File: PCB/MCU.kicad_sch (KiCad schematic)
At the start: 15 parts

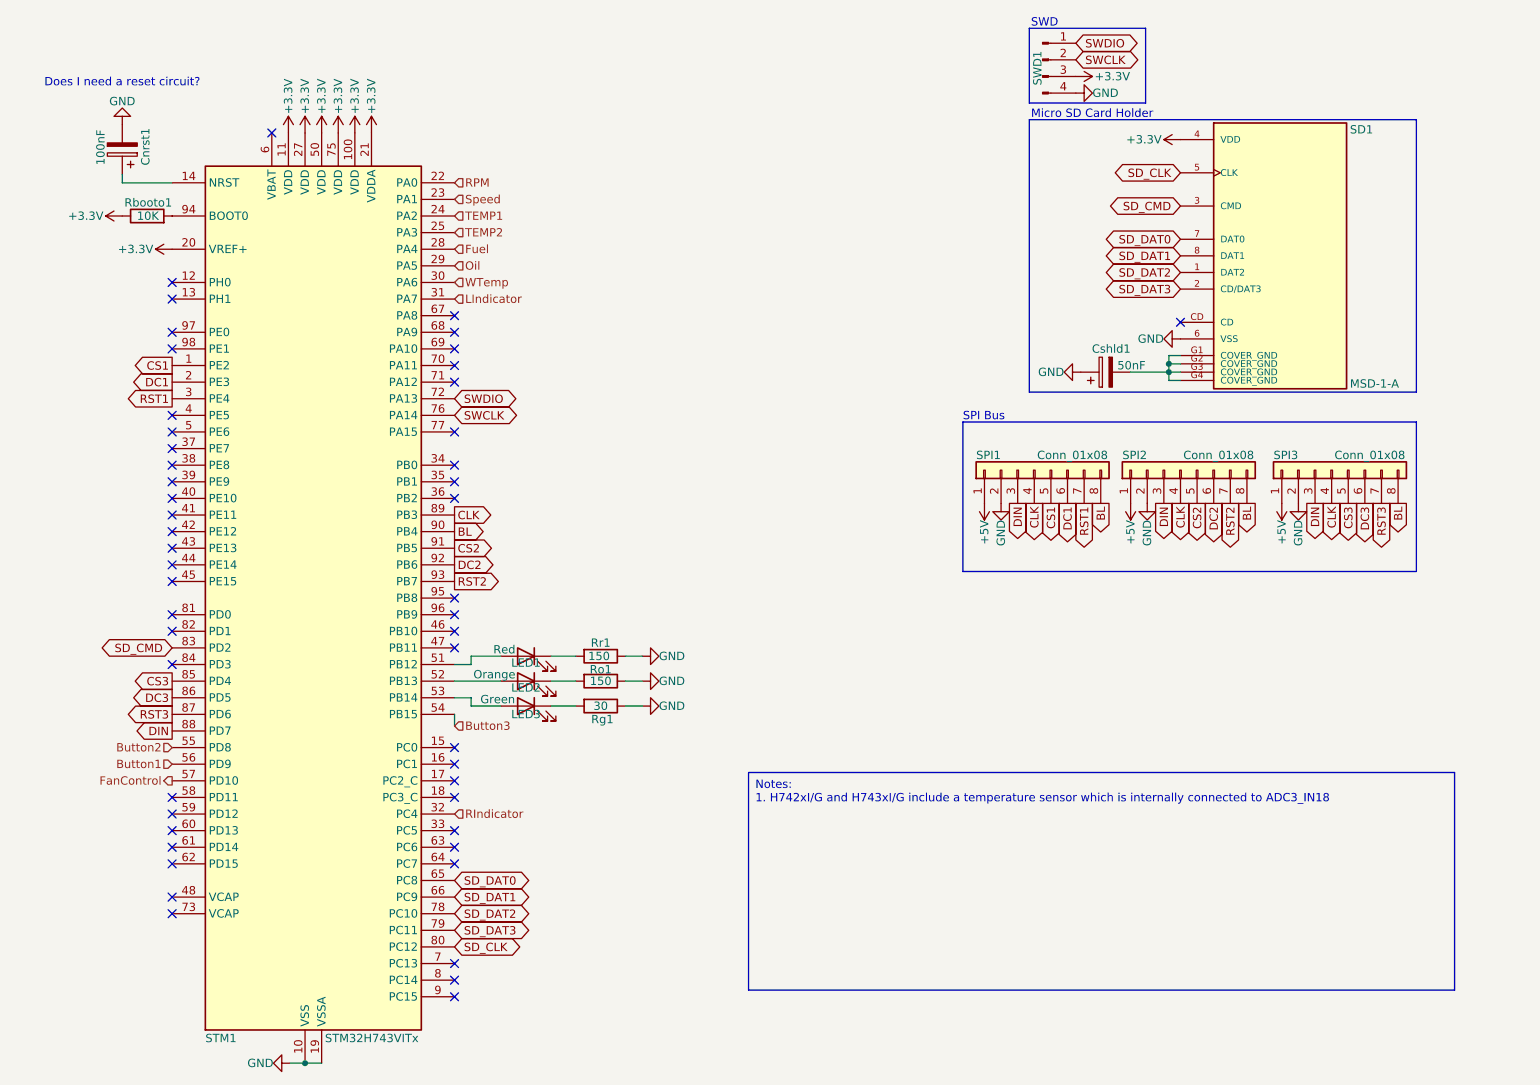
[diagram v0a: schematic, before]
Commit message: Replaced STM32 with ESP32; Addec circuitry for ESP32; Removed LEDs; Added USB-C for flashing
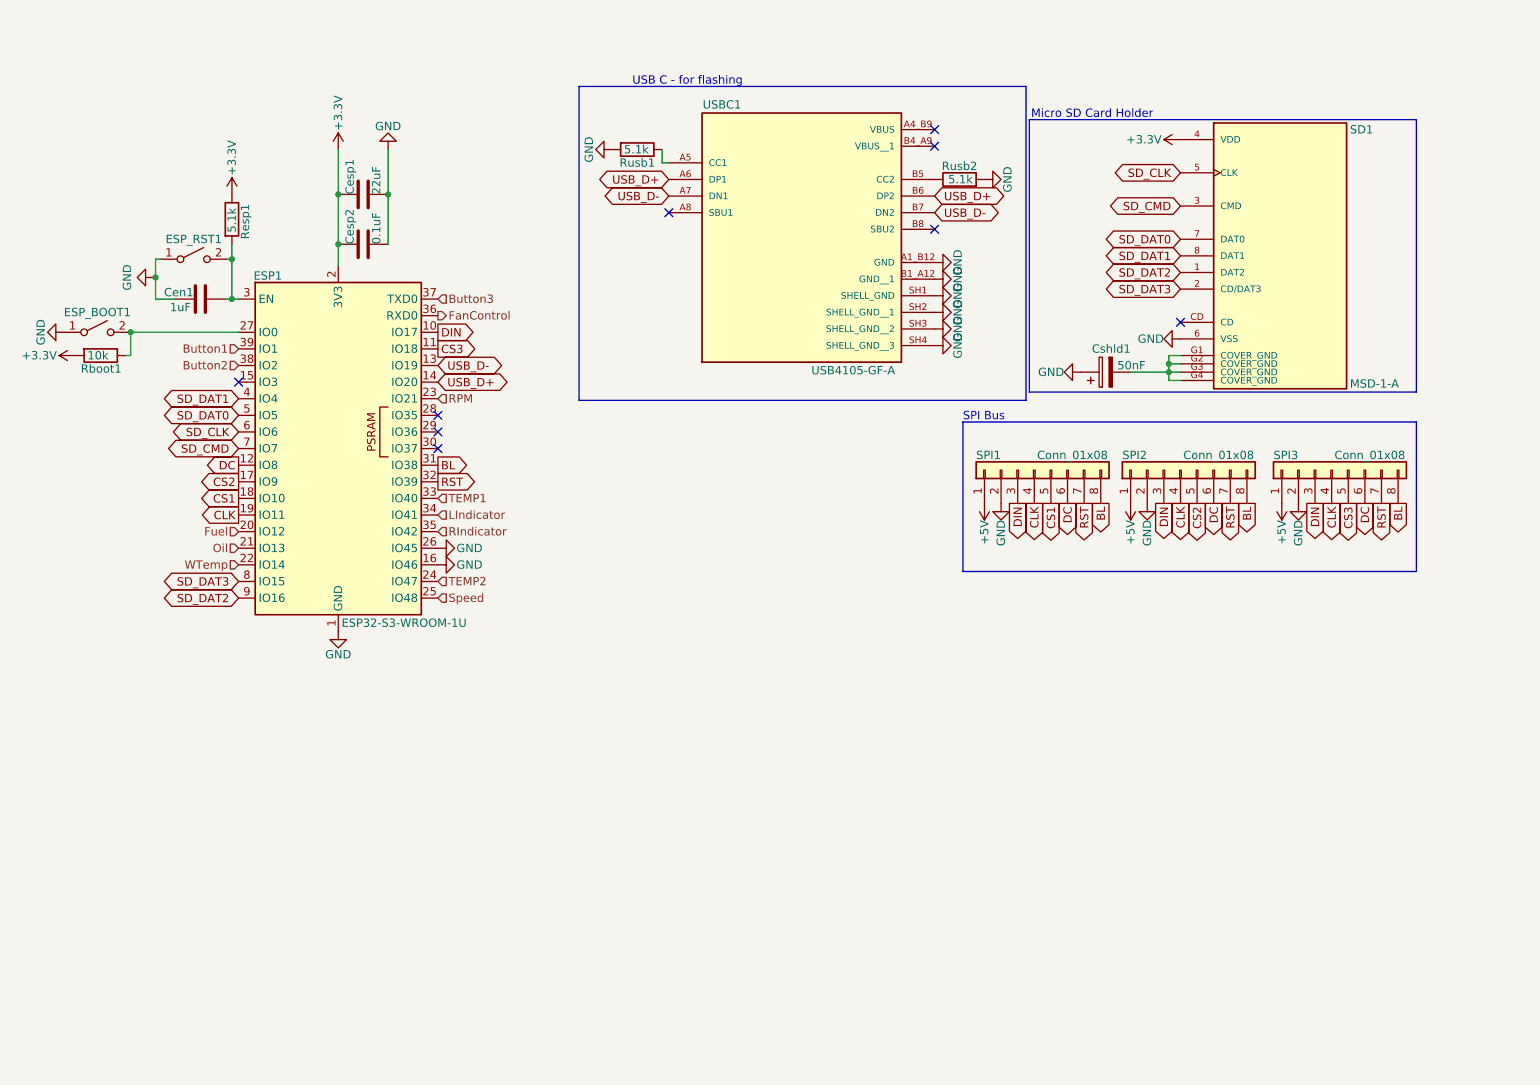
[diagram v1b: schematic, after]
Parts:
- removed Cnrst1: 100nF, Capacitor_SMD:C_0805_2012Metric, symbol Device:C_Polarized
- removed LED1: Red, LED_SMD:LED_0603_1608Metric, symbol Device:LED
- removed LED2: Orange, LED_SMD:LED_0603_1608Metric, symbol Device:LED
- removed LED3: Green, LED_SMD:LED_0603_1608Metric, symbol Device:LED
- removed Rbooto1: 10K, Resistor_SMD:R_0603_1608Metric, symbol Device:R
- removed Rg1: 30, Resistor_SMD:R_0603_1608Metric, symbol Device:R
- removed Ro1, Rr1: 150, Resistor_SMD:R_0603_1608Metric, symbol Device:R
- removed STM1: STM32H743VITx, Package_QFP:LQFP-100_14x14mm_P0.5mm, symbol MCU_ST_STM32H7:STM32H743VITx
- removed SWD1: Conn_01x04_Pin, Connector_PinHeader_2.54mm:PinHeader_1x04_P2.54mm_Vertical, symbol Connector:Conn_01x04_Pin
- added Cen1: 1uF, Capacitor_SMD:C_0805_2012Metric, symbol Device:C
- added Cesp1: 22uF, Capacitor_SMD:C_0805_2012Metric, symbol Device:C
- added Cesp2: 0.1uF, Capacitor_SMD:C_0805_2012Metric, symbol Device:C
- added ESP1: ESP32-S3-WROOM-1U, RF_Module:ESP32-S3-WROOM-1U, symbol RF_Module:ESP32-S3-WROOM-1
- added ESP_BOOT1, ESP_RST1: SW_SPST, button:small_button, symbol Switch:SW_SPST
- added Rboot1: 10k, Resistor_SMD:R_0603_1608Metric, symbol Device:R
- added Resp1, Rusb1, Rusb2: 5.1k, Resistor_SMD:R_0603_1608Metric, symbol Device:R
- added USBC1: USB4105-GF-A, USB-C 2.0:GCT_USB4105-GF-A, symbol USB-C:USB4105-GF-A
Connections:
- net DC2 is gone; now on net DC: SPI2.6 (Pin_6)
- net DC3 is gone; now on net DC: SPI3.6 (Pin_6)
- net RST2 is gone; now on net RST: SPI2.7 (Pin_7)
- net RST3 is gone; now on net RST: SPI3.7 (Pin_7)
- net +3.3V: now also Cesp1.1, Cesp2.1, ESP1.2 (3V3), Rboot1.2, Resp1.1
- net BL: now also ESP1.31 (IO38)
- net Button1: now also ESP1.39 (IO1)
- net Button2: now also ESP1.38 (IO2)
- net Button3: now also ESP1.37 (TXD0)
- net CLK: now also ESP1.19 (IO11)
- net CS1: now also ESP1.18 (IO10)
- net CS2: now also ESP1.17 (IO9)
- net CS3: now also ESP1.11 (IO18)
- net DIN: now also ESP1.10 (IO17)
- net FanControl: now also ESP1.36 (RXD0)
- net Fuel: now also ESP1.20 (IO12)
- net GND: now also Cen1.1, Cesp1.2, Cesp2.2, ESP1.1 (GND), ESP1.16 (IO46), ESP1.26 (IO45), ESP1.40 (GND), ESP1.41 (GND), ESP_BOOT1.1 (A), ESP_RST1.1 (A), Rusb1.2, Rusb2.2, USBC1.A1_B12 (GND), USBC1.B1_A12 (GND__1), USBC1.SH1 (SHELL_GND), USBC1.SH2 (SHELL_GND__1), USBC1.SH3 (SHELL_GND__2), USBC1.SH4 (SHELL_GND__3)
- net LIndicator: now also ESP1.34 (IO41)
- net Oil: now also ESP1.21 (IO13)
- net RIndicator: now also ESP1.35 (IO42)
- net RPM: now also ESP1.23 (IO21)
- net SD_CLK: now also ESP1.6 (IO6)
- net SD_CMD: now also ESP1.7 (IO7)
- net SD_DAT0: now also ESP1.5 (IO5)
- net SD_DAT1: now also ESP1.4 (IO4)
- net SD_DAT2: now also ESP1.9 (IO16)
- net SD_DAT3: now also ESP1.8 (IO15)
- net Speed: now also ESP1.25 (IO48)
- net TEMP1: now also ESP1.33 (IO40)
- net TEMP2: now also ESP1.24 (IO47)
- net WTemp: now also ESP1.22 (IO14)
- net DC1 renamed DC
- net DC: now also ESP1.12 (IO8)
- net RST1 renamed RST
- net RST: now also ESP1.32 (IO39)
- new net: ESP1.27 (IO0), ESP_BOOT1.2 (B), Rboot1.1
- new net: Cen1.2, ESP1.3 (EN), ESP_RST1.2 (B), Resp1.2
- new net: Rusb1.1, USBC1.A5 (CC1)
- new net: Rusb2.1, USBC1.B5 (CC2)
- new net USB_D+: ESP1.14 (IO20), USBC1.A6 (DP1), USBC1.B6 (DP2)
- new net USB_D-: ESP1.13 (IO19), USBC1.A7 (DN1), USBC1.B7 (DN2)
- no-connect marks 50 -> 9
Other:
- note added: "USB C - for flashing"
- note removed: "Does I need a reset circuit?"
- note removed: "SWD"

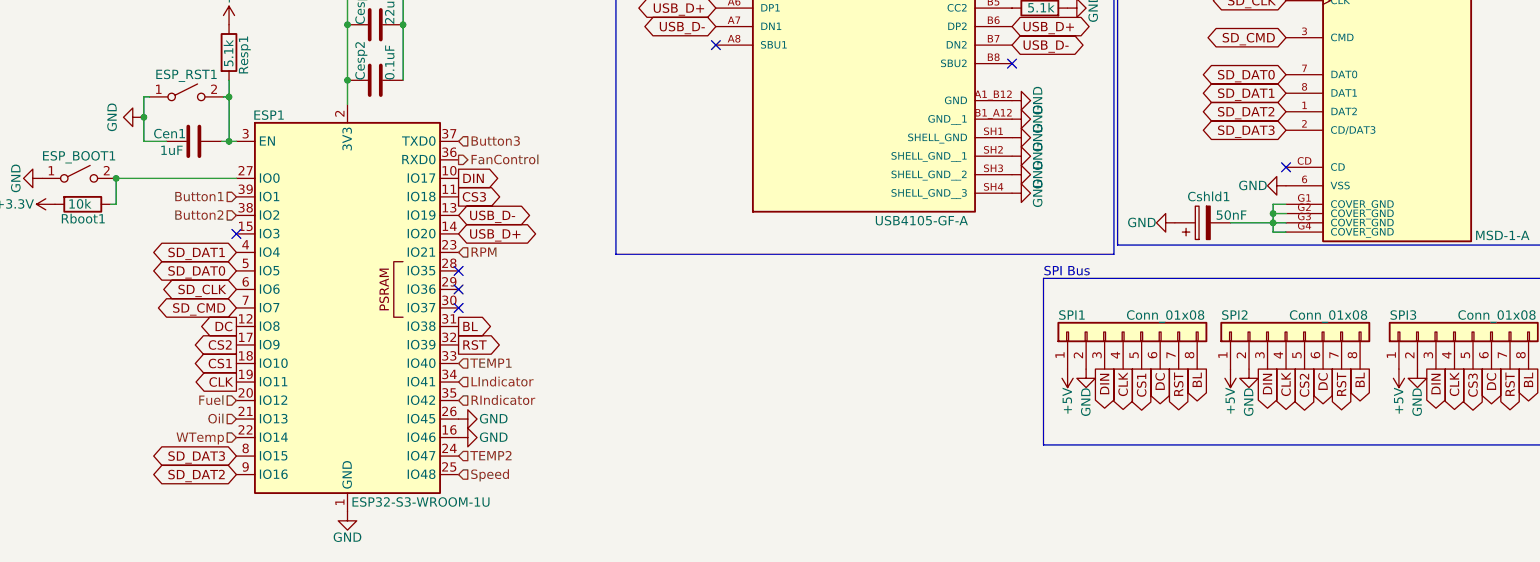
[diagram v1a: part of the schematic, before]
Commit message: Changed PCB design completely; Upgraded 3.3V regulator to 1.5A version; Removed no more needed libaries
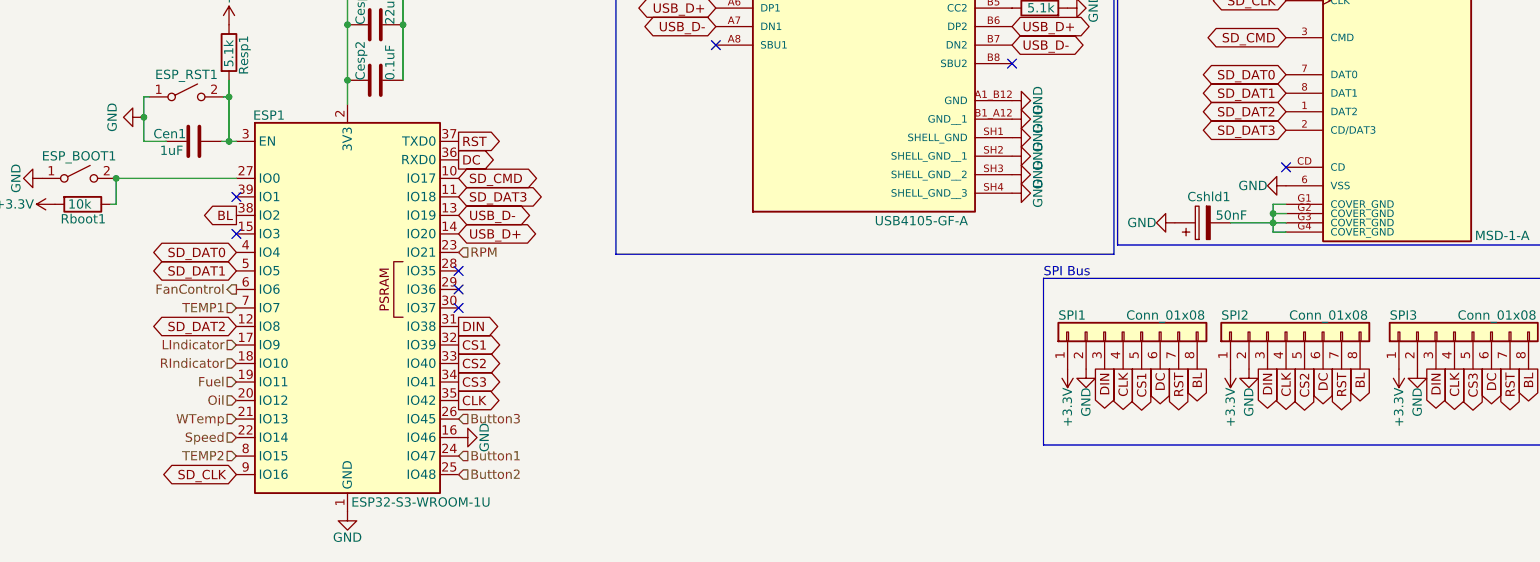
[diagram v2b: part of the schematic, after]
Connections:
- net +5V is gone; now on net +3.3V: SPI1.1 (Pin_1), SPI2.1 (Pin_1), SPI3.1 (Pin_1)
- net BL: now also ESP1.38 (IO2); no longer ESP1.31 (IO38)
- net Button1: now also ESP1.24 (IO47); no longer ESP1.39 (IO1)
- net Button2: now also ESP1.25 (IO48); no longer ESP1.38 (IO2)
- net Button3: now also ESP1.26 (IO45); no longer ESP1.37 (TXD0)
- net CLK: now also ESP1.35 (IO42); no longer ESP1.19 (IO11)
- net CS1: now also ESP1.32 (IO39); no longer ESP1.18 (IO10)
- net CS2: now also ESP1.33 (IO40); no longer ESP1.17 (IO9)
- net CS3: now also ESP1.34 (IO41); no longer ESP1.11 (IO18)
- net DC: now also ESP1.36 (RXD0); no longer ESP1.12 (IO8)
- net DIN: now also ESP1.31 (IO38); no longer ESP1.10 (IO17)
- net FanControl: now also ESP1.6 (IO6); no longer ESP1.36 (RXD0)
- net Fuel: now also ESP1.19 (IO11); no longer ESP1.20 (IO12)
- net GND: no longer ESP1.26 (IO45)
- net LIndicator: now also ESP1.17 (IO9); no longer ESP1.34 (IO41)
- net Oil: now also ESP1.20 (IO12); no longer ESP1.21 (IO13)
- net RIndicator: now also ESP1.18 (IO10); no longer ESP1.35 (IO42)
- net RST: now also ESP1.37 (TXD0); no longer ESP1.32 (IO39)
- net SD_CLK: now also ESP1.9 (IO16); no longer ESP1.6 (IO6)
- net SD_CMD: now also ESP1.10 (IO17); no longer ESP1.7 (IO7)
- net SD_DAT0: now also ESP1.4 (IO4); no longer ESP1.5 (IO5)
- net SD_DAT1: now also ESP1.5 (IO5); no longer ESP1.4 (IO4)
- net SD_DAT2: now also ESP1.12 (IO8); no longer ESP1.9 (IO16)
- net SD_DAT3: now also ESP1.11 (IO18); no longer ESP1.8 (IO15)
- net Speed: now also ESP1.22 (IO14); no longer ESP1.25 (IO48)
- net TEMP1: now also ESP1.7 (IO7); no longer ESP1.33 (IO40)
- net TEMP2: now also ESP1.8 (IO15); no longer ESP1.24 (IO47)
- net WTemp: now also ESP1.21 (IO13); no longer ESP1.22 (IO14)
- no-connect marks 9 -> 10

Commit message: Added pulldown resistors for the buttons;Changed input GPIof button 3;Replaced a few capacitors (BOM); Put temperature sensors on the 3.3V line
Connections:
- net Button3: now also ESP1.39 (IO1); no longer ESP1.26 (IO45)
- net GND: now also ESP1.26 (IO45)
- no-connect marks 10 -> 9
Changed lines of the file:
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@@
 	)
 	(no_connect
-		(at 99.06 67.31)
-	)
-	(no_connect
 		(at 164.846 46.482)
 	)
@@
 		)
 	)
+	(hierarchical_label "Button3"
+		(shape input)
+		(at 99.06 67.31 180)
+		(fields_autoplaced yes)
+		(effects
+			(font
+				(size 1.27 1.27)
+			)
+			(justify right)
+		)
+	)
 	(hierarchical_label "RIndicator"
 		(shape input)
@@
 		)
 	)
-	(hierarchical_label "Button3"
-		(shape input)
-		(at 129.54 97.79 0)
-		(fields_autoplaced yes)
-		(effects
-			(font
-				(size 1.27 1.27)
-			)
-			(justify left)
-		)
-	)
 	(hierarchical_label "Oil"
 		(shape input)
@@
 	)
 	(symbol
+		(lib_id "power:GND")
+		(at 129.54 97.79 90)
+		(unit 1)
+		(exclude_from_sim no)
+		(in_bom yes)
+		(on_board yes)
+		(dnp no)
+		(property "Reference" "#PWR036"
+			(at 135.89 97.79 0)
+			(effects
+				(font
+					(size 1.27 1.27)
+				)
+				(hide yes)
+			)
+		)
+		(property "Value" "GND"
+			(at 134.366 97.79 90)
+			(effects
+				(font
+					(size 1.27 1.27)
+				)
+			)
+		)
+		(property "Footprint" ""
+			(at 129.54 97.79 0)
+			(effects
+				(font
+					(size 1.27 1.27)
+				)
+				(hide yes)
+			)
+		)
+		(property "Datasheet" ""
+			(at 129.54 97.79 0)
+			(effects
+				(font
+					(size 1.27 1.27)
+				)
+				(hide yes)
+			)
+		)
+		(property "Description" "Power symbol creates a global label with name \"GND\" , ground"
+			(at 129.54 97.79 0)
+			(effects
+				(font
+					(size 1.27 1.27)
+				)
+				(hide yes)
+			)
+		)
+		(pin "1"
+		)
+		(instances
+			(project "Leiterkarte-v2"
+				(path "/7159fc5a-6328-470f-acd9-3e0a0aa6e60c/387d92f2-3727-45df-9c4d-1355459e23fb"
+					(reference "#PWR036")
+					(unit 1)
+				)
+			)
+		)
+	)
+	(symbol
 		(lib_id "Device:C")
 		(at 93.218 59.69 90)
@@
 		)
 		(property "Value" "GND"
-			(at 133.096 100.33 0)
+			(at 134.366 100.33 90)
 			(effects
 				(font

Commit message: PCB Version 2.1
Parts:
- added JP1: SolderJumper_2_Open, Jumper:SolderJumper-2_P1.3mm_Open_TrianglePad1.0x1.5mm, symbol Jumper:SolderJumper_2_Open
- added TP13, TP14, TP15, TP16, TP18, TP19, TP20, TP21, TP22, TP23, TP24, TP25, TP26, TP27, TP28, TP29: TestPoint_Small, TestPoint:TestPoint_Pad_D1.0mm, symbol Connector:TestPoint_Small
- SPI1, SPI2, SPI3: footprint Connector_JST:JST_SH_BM08B-SRSS-TB_1x08-1MP_P1.00mm_Vertical -> Connector_JST:JST_XH_S8B-XH-A_1x08_P2.50mm_Horizontal
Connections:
- net BL: now also TP20.1
- net CLK: now also TP16.1
- net CS1: now also TP23.1
- net CS2: now also TP22.1
- net CS3: now also TP21.1
- net DC: now also TP18.1
- net DIN: now also TP15.1
- net Fuel: now also ESP1.21 (IO13); no longer ESP1.19 (IO11)
- net LIndicator: now also ESP1.18 (IO10); no longer ESP1.17 (IO9)
- net RIndicator: now also ESP1.17 (IO9); no longer ESP1.18 (IO10)
- net RST: now also TP19.1
- net SD_CLK: now also TP24.1
- net SD_CMD: now also TP25.1
- net SD_DAT0: now also TP26.1
- net SD_DAT1: now also TP27.1
- net SD_DAT2: now also TP28.1
- net SD_DAT3: now also TP29.1
- net USB_D+: now also TP14.1
- net USB_D-: now also TP13.1
- net WTemp: now also ESP1.19 (IO11); no longer ESP1.21 (IO13)
- net at USBC1.A4_B9 (VBUS): now also USBC1.B4_A9 (VBUS__1), JP1.1 (A)
- new net +5V: JP1.2 (B)
- no-connect marks 9 -> 7
